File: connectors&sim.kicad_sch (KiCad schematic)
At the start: 30 parts, among them J1 43650-0516, J2 43650-0516, J3 43650-0216, J4 43650-0416, J5 43045-1013, J6 43650-0616, J7 43650-0216

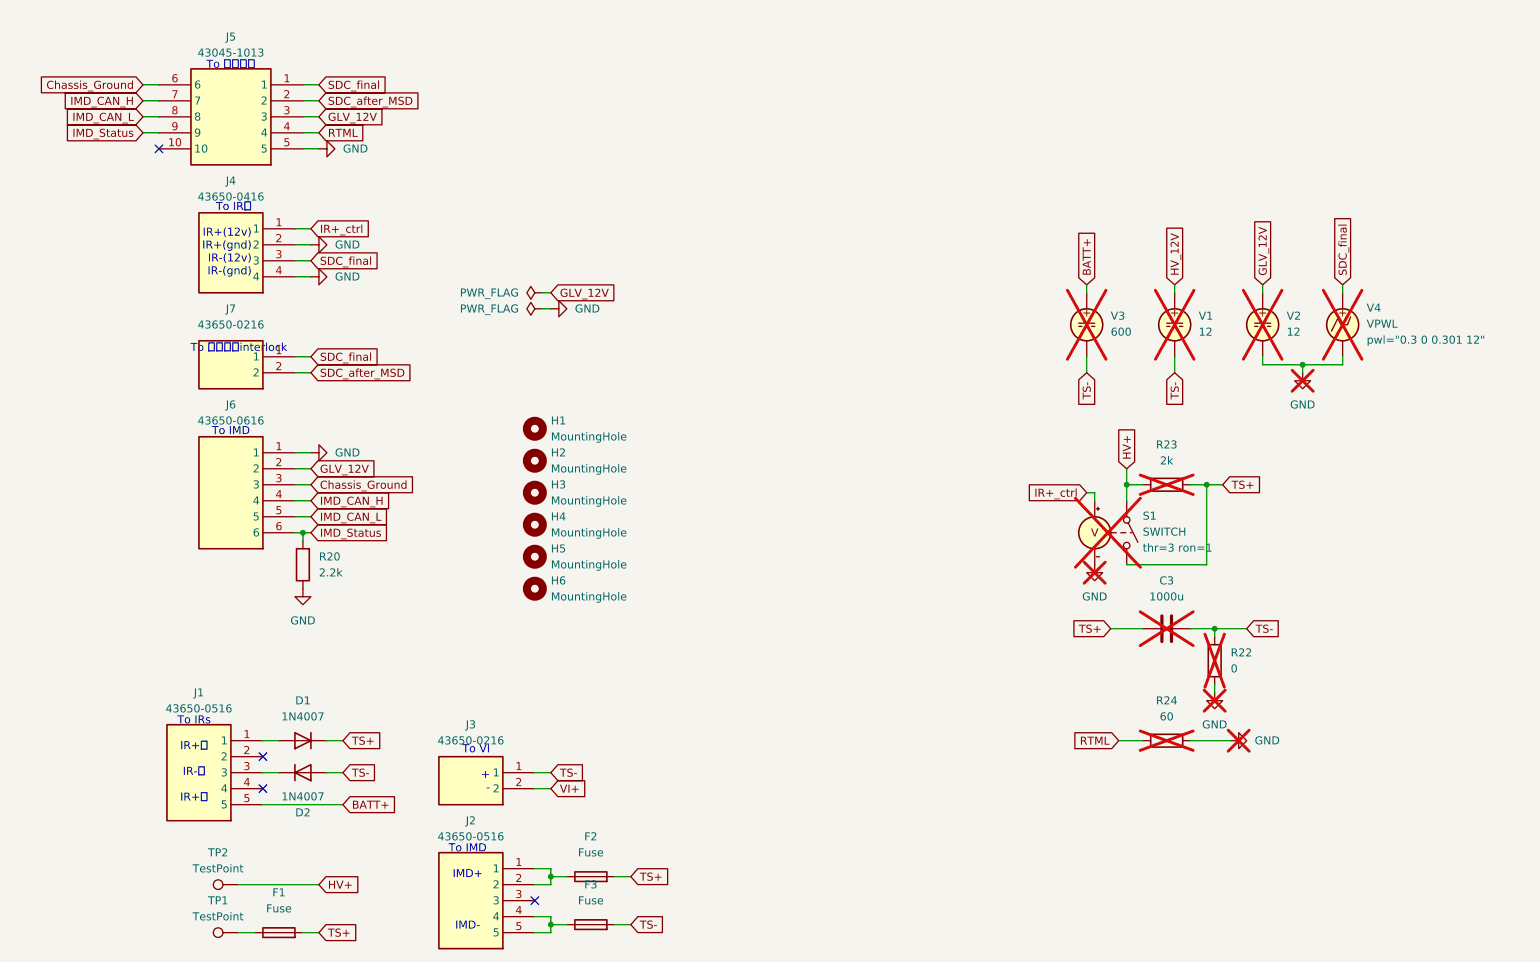
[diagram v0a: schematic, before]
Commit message: J5 reorientation
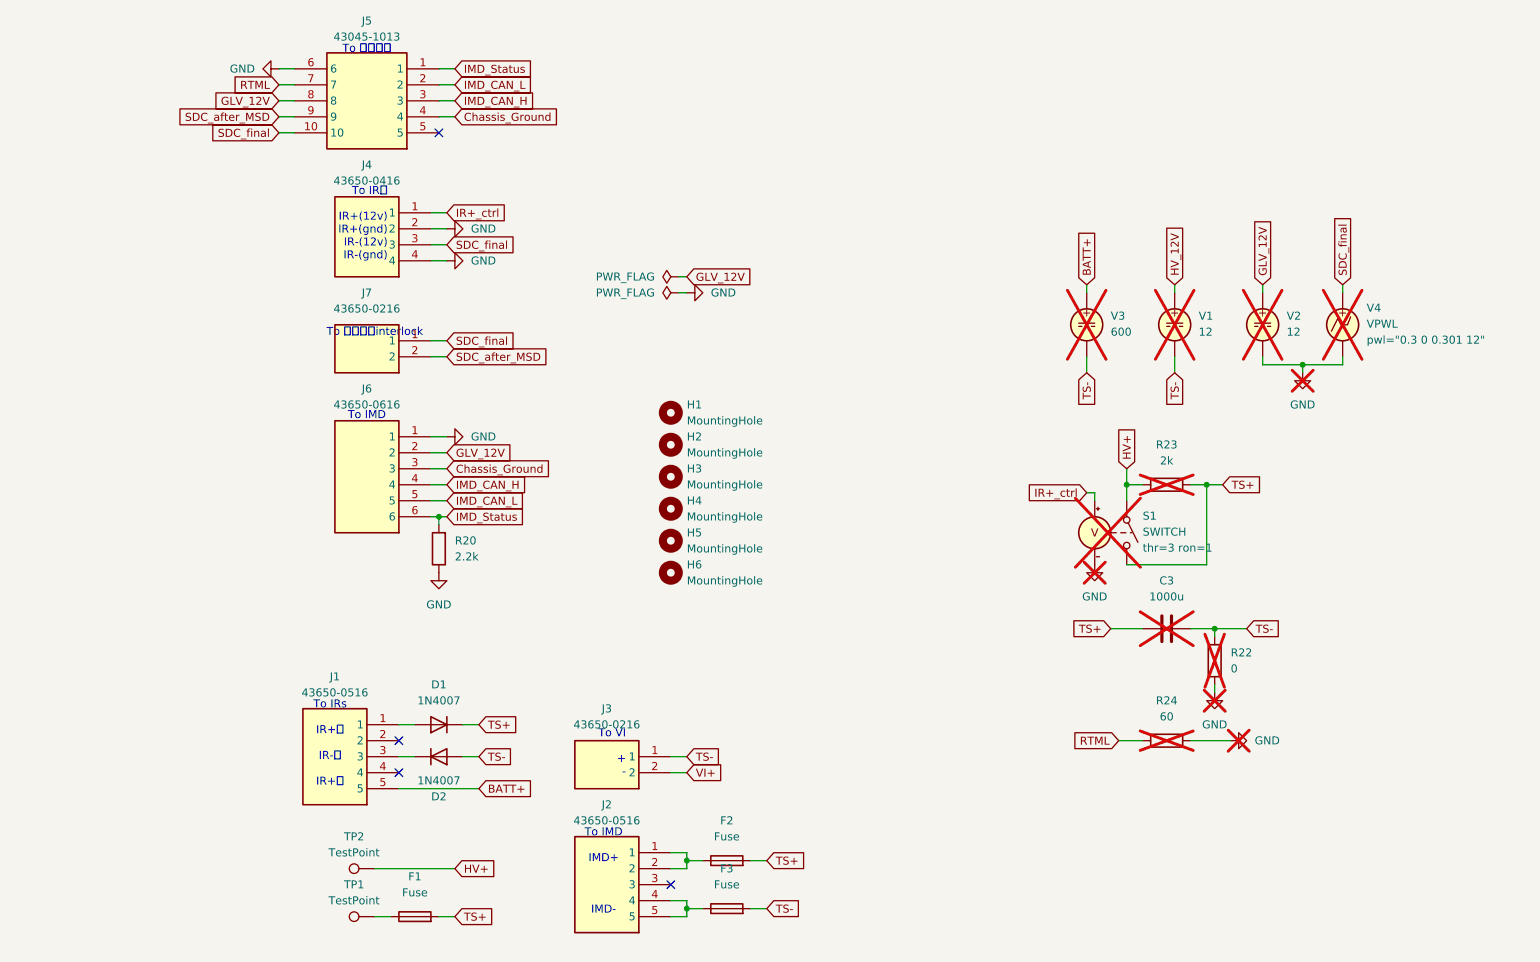
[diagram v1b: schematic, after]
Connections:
- net Chassis_Ground: now also J5.4; no longer J5.6
- net GLV_12V: now also J5.8; no longer J5.3
- net GND: now also J5.6; no longer J5.5
- net IMD_CAN_H: now also J5.3; no longer J5.7
- net IMD_CAN_L: now also J5.2; no longer J5.8
- net IMD_Status: now also J5.1; no longer J5.9
- net RTML: now also J5.7; no longer J5.4
- net SDC_after_MSD: now also J5.9; no longer J5.2
- net SDC_final: now also J5.10; no longer J5.1
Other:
- moved on the sheet: D1, D2, F1, F2, F3, H1, H2, H3, H4, H5, H6, J1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

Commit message: find and fix test errors, some improvement
1. remove onboard fuse (now is inline)
2. change RTML nmos to pmos (to make nmos on, RTML only have V_G-V_th=10V, which is not enough to drive RTML)
3. new voltage divider config (resistors tolerance is matter, <1% is better)
4. add IR+_ctrl signal output to J5
5. J7 is now used for powering Arduino rather than bridging interlock signal (SDC_after_MSD is removed from J5 as well)
6. explain the working principle on sch
7. move to kicad 10
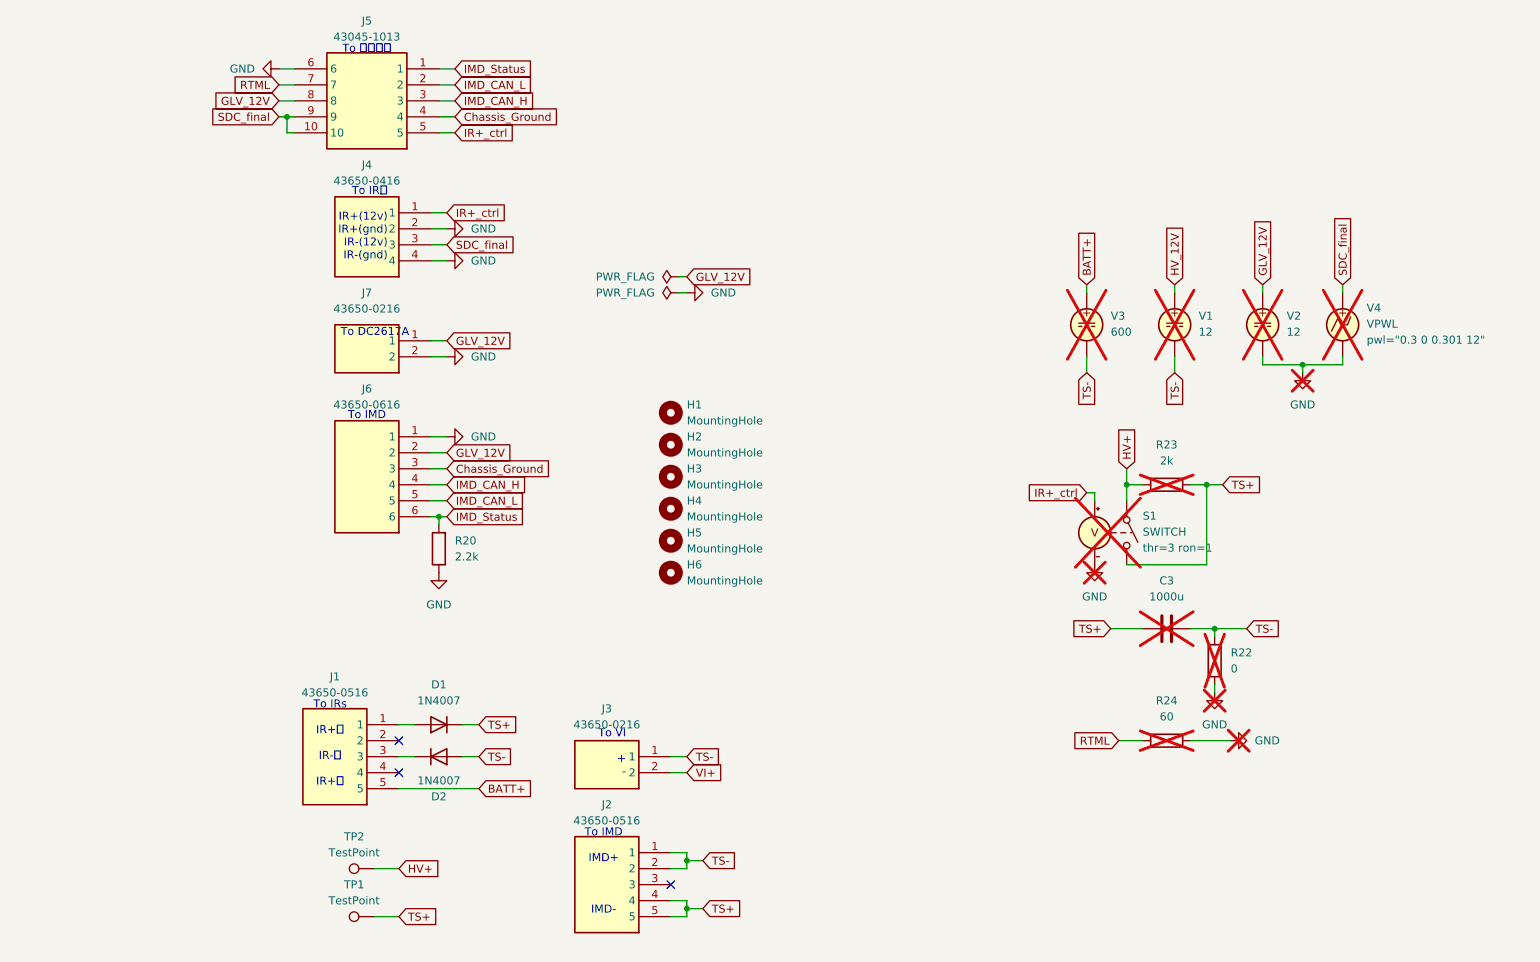
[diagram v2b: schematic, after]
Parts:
- removed F1, F2, F3: Fuse, Resistor_THT:R_Axial_DIN0516_L15.5mm_D5.0mm_P30.48mm_Horizontal, symbol Device:Fuse
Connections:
- net GLV_12V: now also J7.1
- net GND: now also J7.2
- net IR+_ctrl: now also J5.5
- net SDC_final: now also J5.9; no longer J7.1
- net TS+: now also J2.4, J2.5, TP1.1
- net TS-: now also J2.1, J2.2
- removed net SDC_after_MSD: J5.9, J7.2
- no-connect marks 4 -> 3
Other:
- note added: "To DC2617A"
- note removed: "To 高壓接頭interlock"
